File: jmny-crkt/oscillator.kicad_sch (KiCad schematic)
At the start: 9 parts, among them Q1 BC847, Q2 BC847, Q3 2N7002

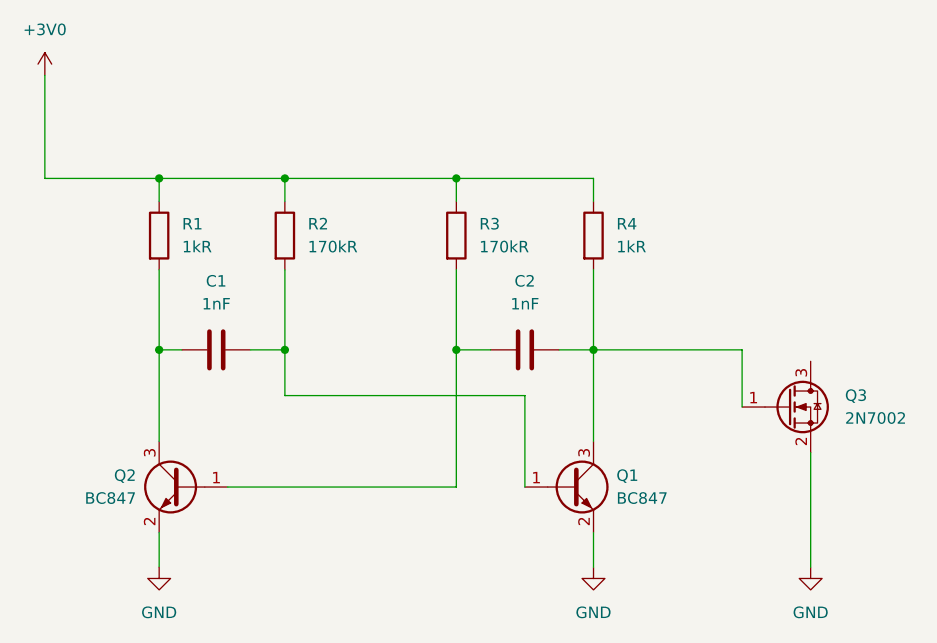
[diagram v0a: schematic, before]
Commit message: Made some progress on the BQ25505 in the old schematic. Will polish it off and import into new project next.
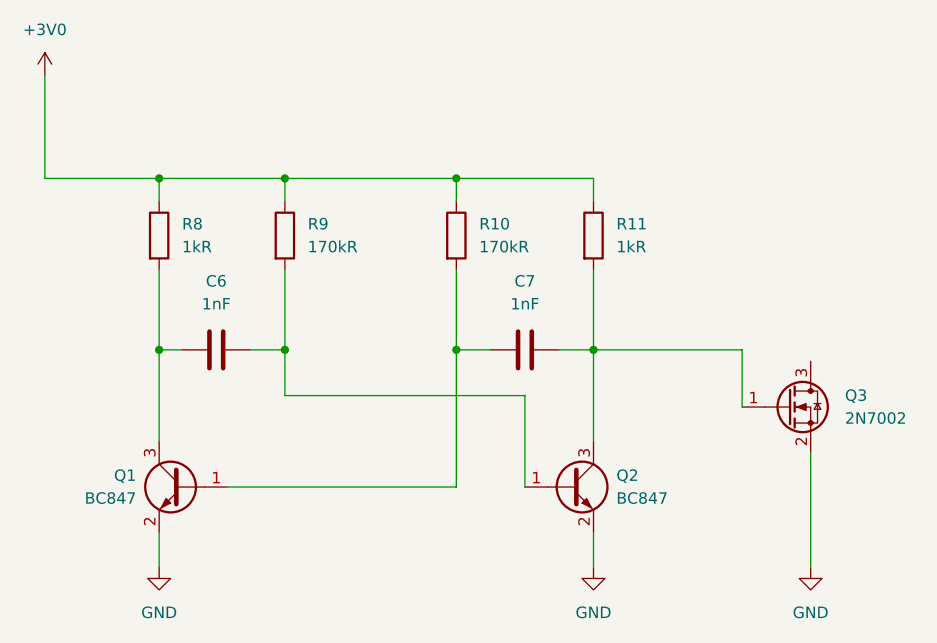
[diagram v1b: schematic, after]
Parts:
- renumbered C1 to C6, C2 to C7, Q2 to Q1, Q1 to Q2, R3 to R10, R4 to R11, R1 to R8, R2 to R9
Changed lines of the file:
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@@
 		(dnp no)
 		(fields_autoplaced yes)
-		(property "Reference" "R4"
+		(property "Reference" "R11"
 			(at 130.81 63.4999 0)
 			(show_name no)
@@
 			(project "jmny-crkt"
 				(path "/70668a17-ad5c-449f-8bac-331355754e01/71bba9b9-5db9-406e-9116-667727c696c3"
-					(reference "R4")
+					(reference "R11")
 					(unit 1)
 				)
@@
 		(dnp no)
 		(fields_autoplaced yes)
-		(property "Reference" "#PWR01"
+		(property "Reference" "#PWR09"
 			(at 80.01 107.95 0)
 			(hide yes)
@@
 			(project "jmny-crkt"
 				(path "/70668a17-ad5c-449f-8bac-331355754e01/71bba9b9-5db9-406e-9116-667727c696c3"
-					(reference "#PWR01")
+					(reference "#PWR09")
 					(unit 1)
 				)
@@
 		(dnp no)
 		(fields_autoplaced yes)
-		(property "Reference" "Q1"
+		(property "Reference" "Q2"
 			(at 130.81 91.4399 0)
 			(show_name no)
@@
 			(project "jmny-crkt"
 				(path "/70668a17-ad5c-449f-8bac-331355754e01/71bba9b9-5db9-406e-9116-667727c696c3"
-					(reference "Q1")
+					(reference "Q2")
 					(unit 1)
 				)
@@
 		(dnp no)
 		(fields_autoplaced yes)
-		(property "Reference" "R2"
+		(property "Reference" "R9"
 			(at 96.52 63.4999 0)
 			(show_name no)
@@
 			(project "jmny-crkt"
 				(path "/70668a17-ad5c-449f-8bac-331355754e01/71bba9b9-5db9-406e-9116-667727c696c3"
-					(reference "R2")
+					(reference "R9")
 					(unit 1)
 				)
@@
 		(dnp no)
 		(fields_autoplaced yes)
-		(property "Reference" "#PWR04"
+		(property "Reference" "#PWR011"
 			(at 152.4 107.95 0)
 			(hide yes)
@@
 			(project "jmny-crkt"
 				(path "/70668a17-ad5c-449f-8bac-331355754e01/71bba9b9-5db9-406e-9116-667727c696c3"
-					(reference "#PWR04")
+					(reference "#PWR011")
 					(unit 1)
 				)
@@
 		(dnp no)
 		(fields_autoplaced yes)
-		(property "Reference" "#PWR02"
+		(property "Reference" "#PWR010"
 			(at 128.27 107.95 0)
 			(hide yes)
@@
 			(project "jmny-crkt"
 				(path "/70668a17-ad5c-449f-8bac-331355754e01/71bba9b9-5db9-406e-9116-667727c696c3"
-					(reference "#PWR02")
+					(reference "#PWR010")
 					(unit 1)
 				)
@@
 		(in_pos_files yes)
 		(dnp no)
-		(property "Reference" "Q2"
+		(property "Reference" "Q1"
 			(at 77.47 91.4399 0)
 			(show_name no)
@@
 			(project "jmny-crkt"
 				(path "/70668a17-ad5c-449f-8bac-331355754e01/71bba9b9-5db9-406e-9116-667727c696c3"
-					(reference "Q2")
+					(reference "Q1")
 					(unit 1)
 				)
@@
 		(dnp no)
 		(fields_autoplaced yes)
-		(property "Reference" "R3"
+		(property "Reference" "R10"
 			(at 115.57 63.4999 0)
 			(show_name no)
@@
 			(project "jmny-crkt"
 				(path "/70668a17-ad5c-449f-8bac-331355754e01/71bba9b9-5db9-406e-9116-667727c696c3"
-					(reference "R3")
+					(reference "R10")
 					(unit 1)
 				)
@@
 		(dnp no)
 		(fields_autoplaced yes)
-		(property "Reference" "R1"
+		(property "Reference" "R8"
 			(at 82.55 63.4999 0)
 			(show_name no)
@@
 			(project "jmny-crkt"
 				(path "/70668a17-ad5c-449f-8bac-331355754e01/71bba9b9-5db9-406e-9116-667727c696c3"
-					(reference "R1")
+					(reference "R8")
 					(unit 1)
 				)
@@
 		(dnp no)
 		(fields_autoplaced yes)
-		(property "Reference" "C1"
+		(property "Reference" "C6"
 			(at 86.36 69.85 90)
 			(show_name no)
@@
 			(project "jmny-crkt"
 				(path "/70668a17-ad5c-449f-8bac-331355754e01/71bba9b9-5db9-406e-9116-667727c696c3"
-					(reference "C1")
+					(reference "C6")
 					(unit 1)
 				)
@@
 		(dnp no)
 		(fields_autoplaced yes)
-		(property "Reference" "#PWR03"
+		(property "Reference" "#PWR08"
 			(at 67.31 50.8 0)
 			(hide yes)
@@
 			(project "jmny-crkt"
 				(path "/70668a17-ad5c-449f-8bac-331355754e01/71bba9b9-5db9-406e-9116-667727c696c3"
-					(reference "#PWR03")
+					(reference "#PWR08")
 					(unit 1)
 				)
@@
 		(dnp no)
 		(fields_autoplaced yes)
-		(property "Reference" "C2"
+		(property "Reference" "C7"
 			(at 120.65 69.85 90)
 			(show_name no)
@@
 			(project "jmny-crkt"
 				(path "/70668a17-ad5c-449f-8bac-331355754e01/71bba9b9-5db9-406e-9116-667727c696c3"
-					(reference "C2")
-					(unit 1)
-				)
+					(reference "C7")
+					(unit 1)
+				)
